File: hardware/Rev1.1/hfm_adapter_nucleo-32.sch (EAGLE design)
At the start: 50 parts, among them IC1 NUCLEO-G431KB, IC10 OPA2992D, IC11 OPA2172D, IC2 M24M02, IC3 IP4234CZ6,115, IC4 LPS25HBTR, IC6 SRV05-4MR6T1GTSSOP6, IC7 TLE4252D, IC8 TLE42764DV, IC9 ADR01_02_03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

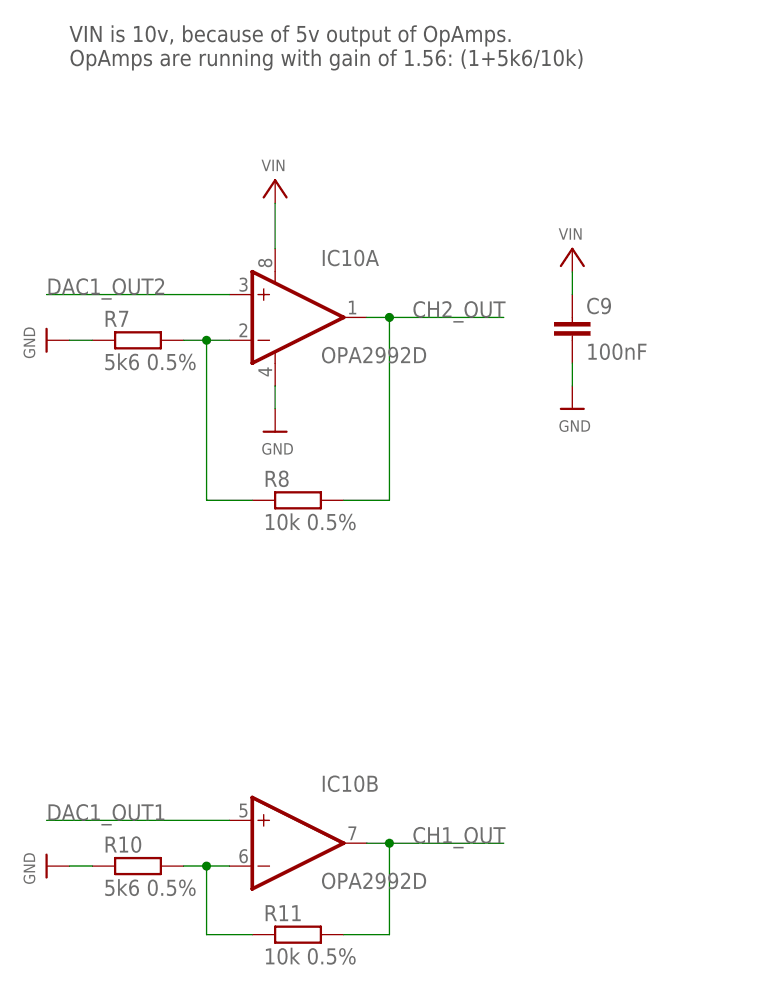
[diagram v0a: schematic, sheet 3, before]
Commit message: amplification factor corrected
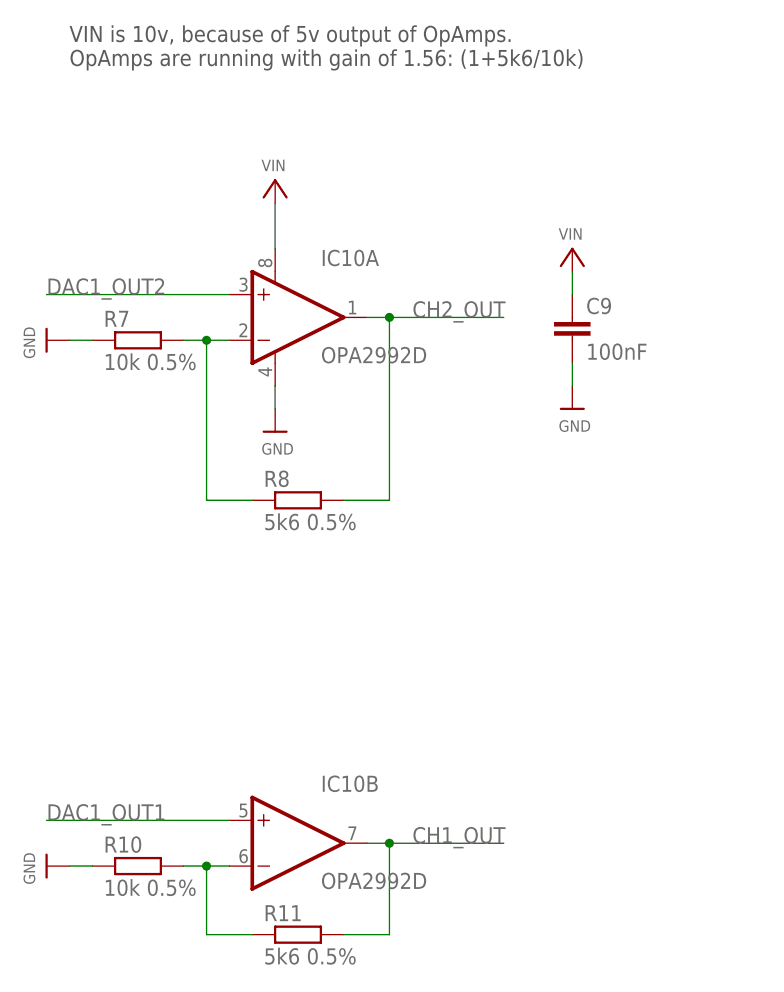
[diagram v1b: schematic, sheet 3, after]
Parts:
- R10, R7: value 5k6 0.5% -> 10k 0.5%
- R11, R8: value 10k 0.5% -> 5k6 0.5%
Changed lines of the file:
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@@
 <part name="U$37" library="microbuilder" deviceset="3.3V" device=""/>
 <part name="U$39" library="microbuilder" deviceset="GND" device=""/>
-<part name="R7" library="rcl" library_urn="urn:adsk.eagle:library:334" deviceset="R-EU_" device="R0805" package3d_urn="urn:adsk.eagle:package:23553/2" value="5k6 0.5%"/>
-<part name="R8" library="rcl" library_urn="urn:adsk.eagle:library:334" deviceset="R-EU_" device="R0805" package3d_urn="urn:adsk.eagle:package:23553/2" value="10k 0.5%"/>
-<part name="R10" library="rcl" library_urn="urn:adsk.eagle:library:334" deviceset="R-EU_" device="R0805" package3d_urn="urn:adsk.eagle:package:23553/2" value="5k6 0.5%"/>
-<part name="R11" library="rcl" library_urn="urn:adsk.eagle:library:334" deviceset="R-EU_" device="R0805" package3d_urn="urn:adsk.eagle:package:23553/2" value="10k 0.5%"/>
+<part name="R7" library="rcl" library_urn="urn:adsk.eagle:library:334" deviceset="R-EU_" device="R0805" package3d_urn="urn:adsk.eagle:package:23553/2" value="10k 0.5%"/>
+<part name="R8" library="rcl" library_urn="urn:adsk.eagle:library:334" deviceset="R-EU_" device="R0805" package3d_urn="urn:adsk.eagle:package:23553/2" value="5k6 0.5%"/>
+<part name="R10" library="rcl" library_urn="urn:adsk.eagle:library:334" deviceset="R-EU_" device="R0805" package3d_urn="urn:adsk.eagle:package:23553/2" value="10k 0.5%"/>
+<part name="R11" library="rcl" library_urn="urn:adsk.eagle:library:334" deviceset="R-EU_" device="R0805" package3d_urn="urn:adsk.eagle:package:23553/2" value="5k6 0.5%"/>
 <part name="U$43" library="microbuilder" deviceset="GND" device=""/>
 <part name="U$44" library="microbuilder" deviceset="GND" device=""/>
